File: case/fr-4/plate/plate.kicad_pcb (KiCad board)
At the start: 2 copper layers, 152.3 x 104.7 mm, 28 parts, among them SW1 SW_Push, SW10 SW_Push, SW11 SW_Push, SW12 SW_Push, SW13 SW_Push, SW14 SW_Push, SW15 SW_Push, SW16 SW_Push, SW17 SW_Push, SW18 SW_Push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

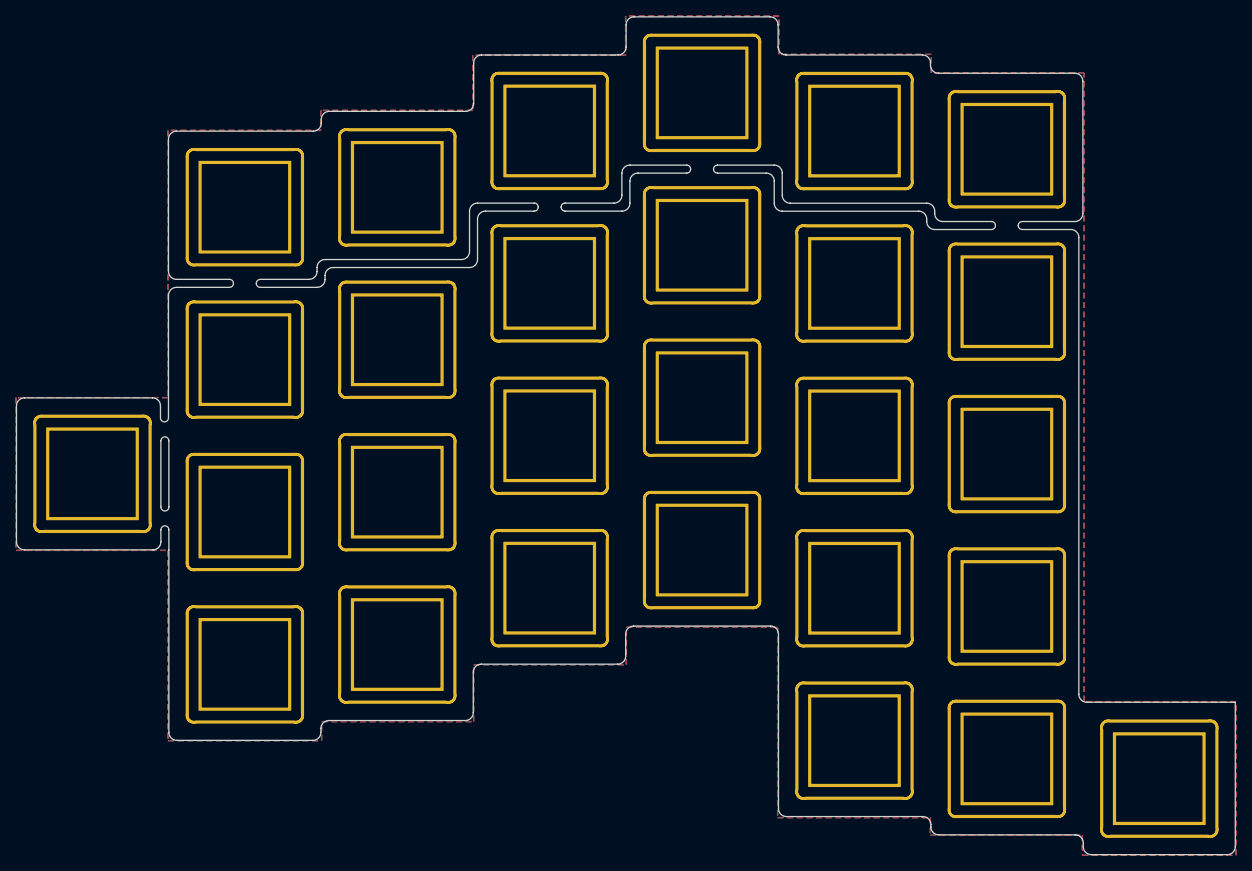
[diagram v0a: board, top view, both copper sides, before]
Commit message: Add holes for mount
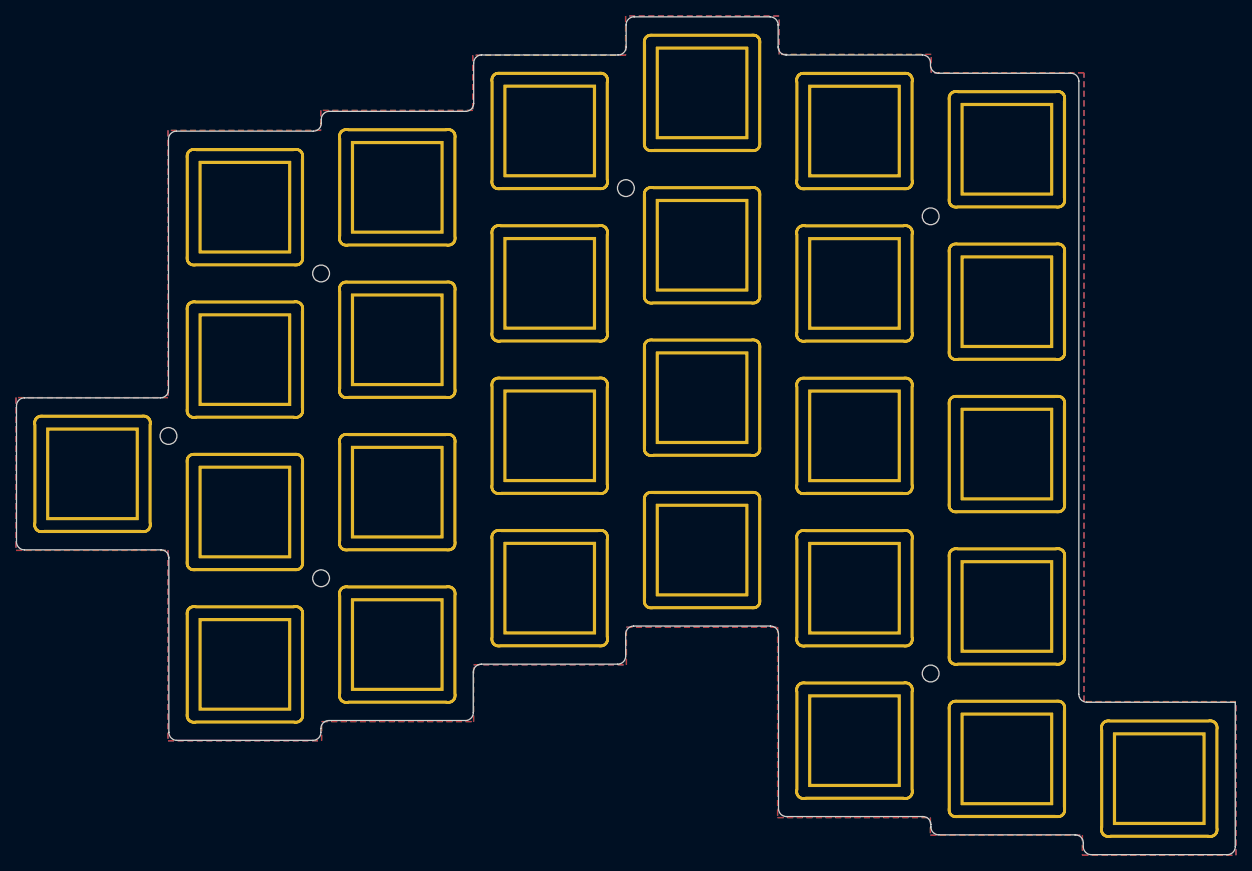
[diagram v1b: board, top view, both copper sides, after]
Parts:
- added REF**: MountingHole_2.1mm, MountingHole:MountingHole_2.1mm, F.Cu at (74.5, 88.9)
- added REF**: MountingHole_2.1mm, MountingHole:MountingHole_2.1mm, F.Cu at (93.5, 106.7)
- added REF**: MountingHole_2.1mm, MountingHole:MountingHole_2.1mm, F.Cu at (93.5, 68.6)
- added REF**: MountingHole_2.1mm, MountingHole:MountingHole_2.1mm, F.Cu at (131.6, 58.0)
- added REF**: MountingHole_2.1mm, MountingHole:MountingHole_2.1mm, F.Cu at (169.7, 61.5)
- added REF**: MountingHole_2.1mm, MountingHole:MountingHole_2.1mm, F.Cu at (169.7, 118.6)
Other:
- outline, holes or cut-outs redrawn

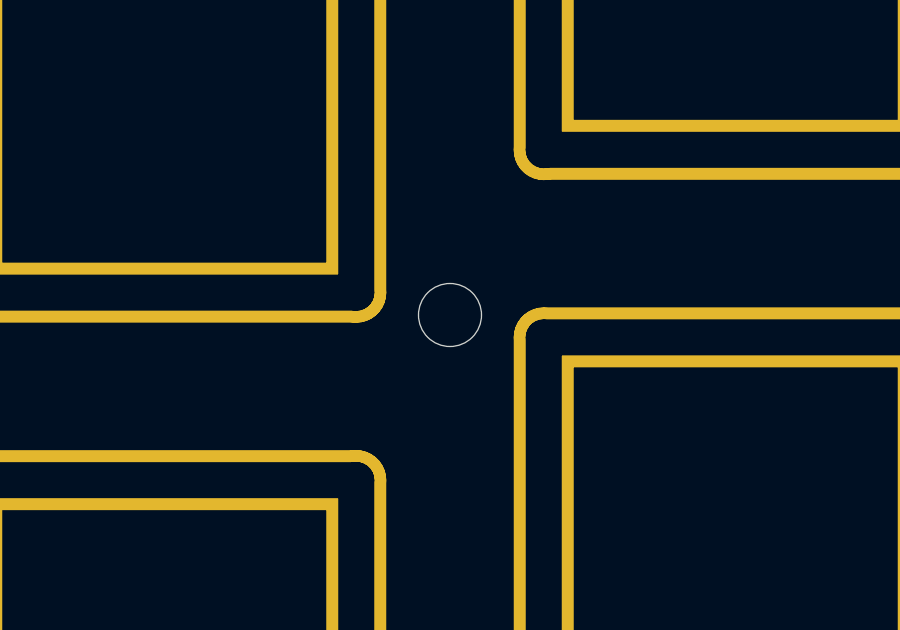
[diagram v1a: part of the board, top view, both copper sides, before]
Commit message: Remove mount hole
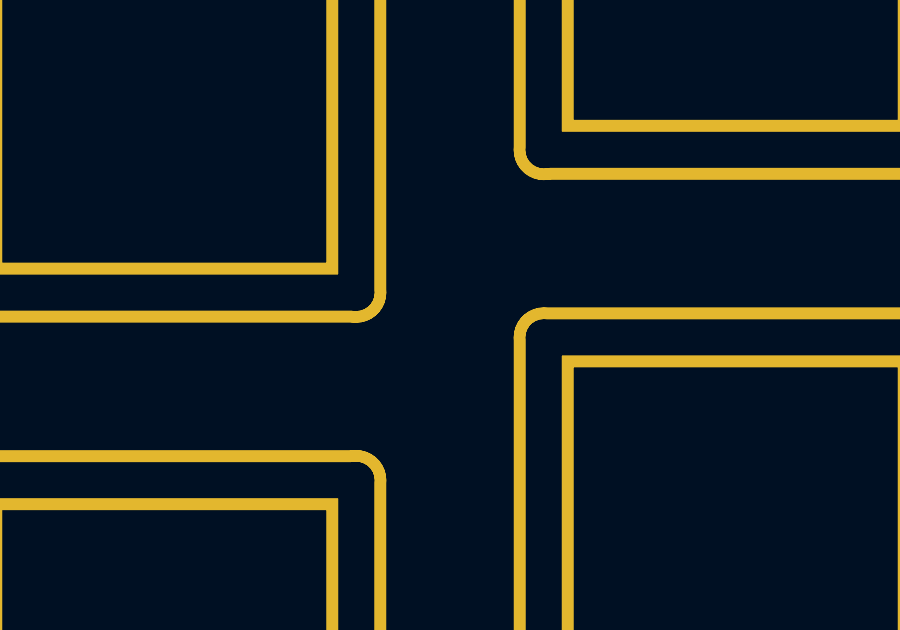
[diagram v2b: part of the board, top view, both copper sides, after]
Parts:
- removed the REF** at (131.6, 58.0)
